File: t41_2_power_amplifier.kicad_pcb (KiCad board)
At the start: 2 copper layers, 69.5 x 93 mm, 52 parts, among them J1 5-1814832-1, J2 5-1814832-1, J3 B2B-XH-A_LF__SN_, J5 Screw_Terminal_01x02, Q1 Q_NMOS_GSD, Q3 Q_NMOS_GSD, T1 Transformer_1P_SS, T2 Transformer_1P_1S, T3 Transformer_1P_1S, U1 MCP1802x-xx02xOT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

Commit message: Version 1.7, release version to fab.
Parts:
- removed U1: MCP1802x-xx02xOT, Package_TO_SOT_SMD:SOT-23-5
- added R10: 2.2k, Resistor_SMD:R_1206_3216Metric, F.Cu at (143.9, 108.5)
- added U3: MCP1804x-A002xOT, Package_TO_SOT_SMD:SOT-23-5, F.Cu at (133.6, 113.6)
- C11: value 0.1uF -> 0.01uF
- C14: value 1uF -> 0.1uF
- moved C13 1.12 mm to (171.9, 116.3)
- moved C2 1.10 mm to (171.9, 113.2)
- moved R9 0.99 mm to (143.9, 111.5)
- moved C9 0.14 mm to (174.2, 121.4)
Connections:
- R9 pad 1: GND -> Net-(R10-Pad2)
- U2 pad 4: /TXRX -> GND
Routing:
- net Net-(R10-Pad2): track 0.00 -> 3.00 mm
- net /TXRX: track 22.8 -> 20.9 mm
- net Net-(U2-*OUT): track 19.8 -> 21.3 mm
- net Net-(U2-SET): track 5.57 -> 6.48 mm
- net GND: vias 122 -> 123
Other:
- board text added: "10 VOLTS"
- board text added: "V1.7"
- board text removed: "8 VOLTS"
- board text removed: "V1.6"

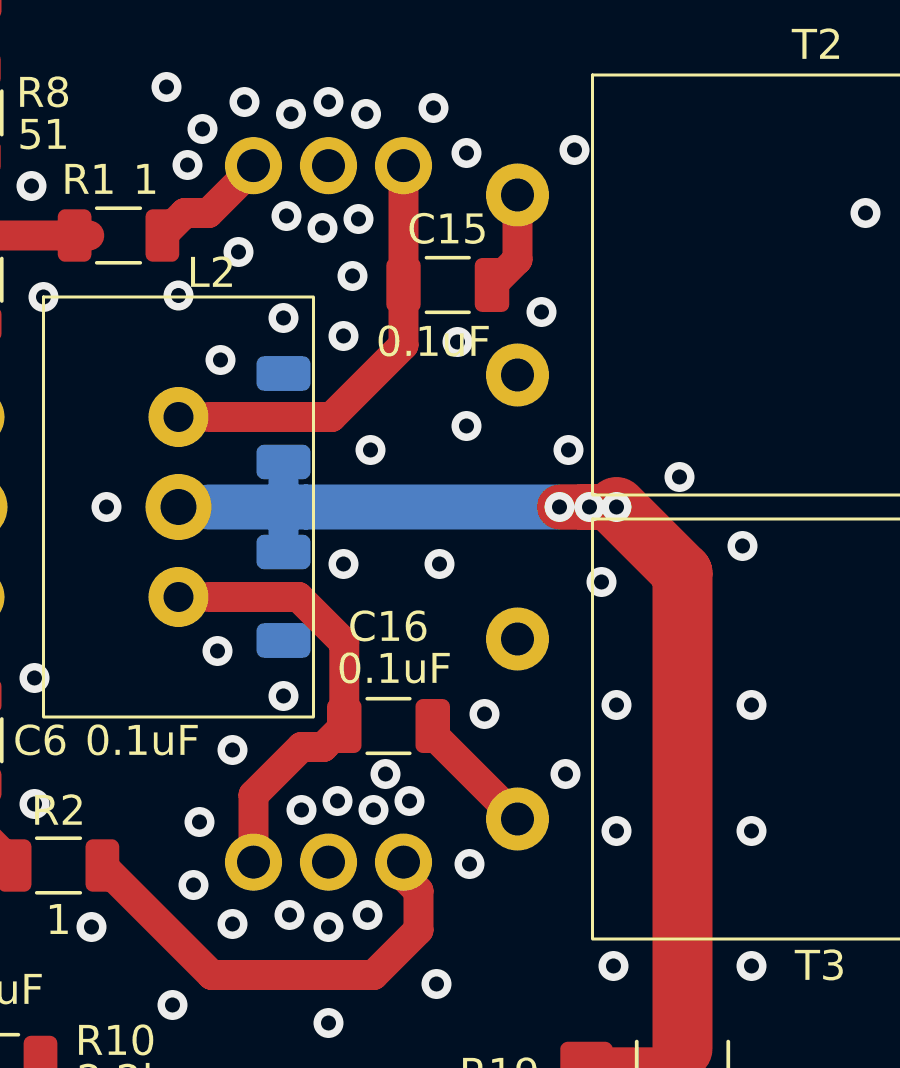
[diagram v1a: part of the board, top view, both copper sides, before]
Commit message: Added output tuning capacitor.
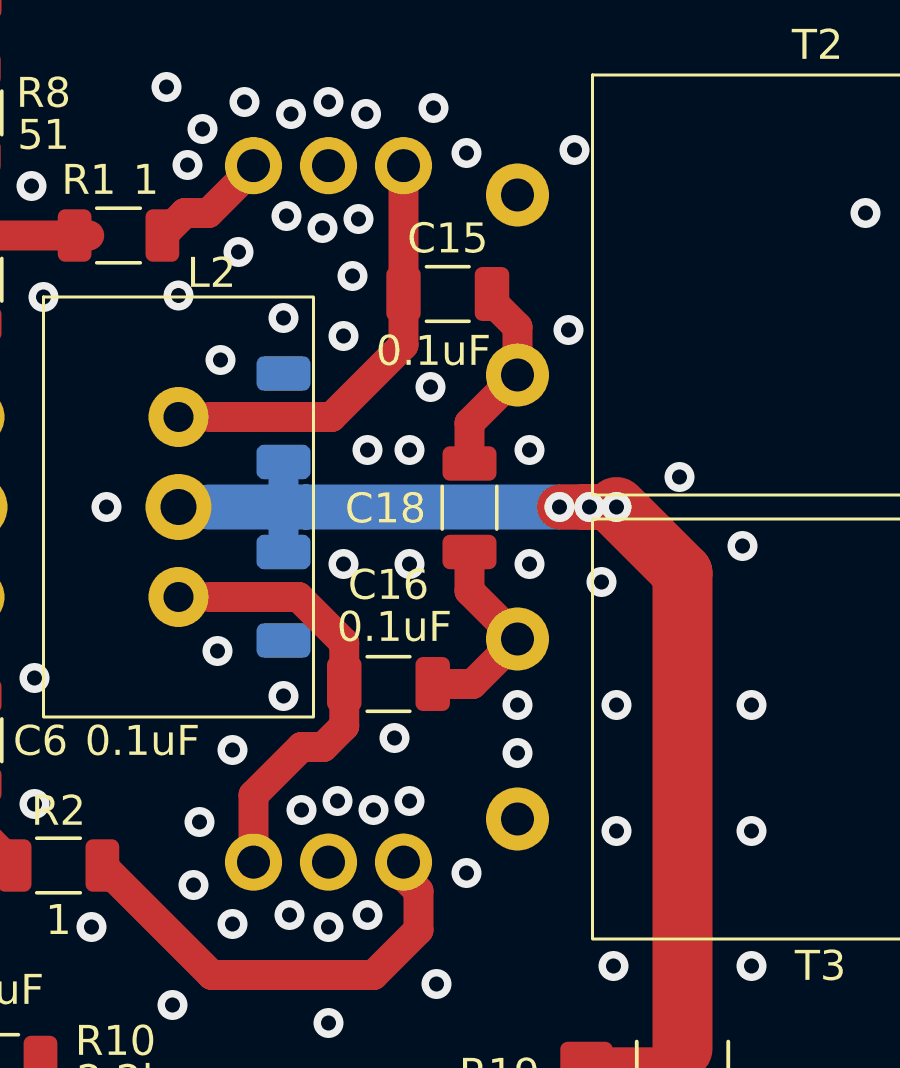
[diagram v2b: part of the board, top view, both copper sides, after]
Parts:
- added C18: 0.1uF, Capacitor_SMD:C_1206_3216Metric, F.Cu at (159.7, 90.0)
- moved C16 1.40 mm to (157.0, 95.9)
- moved C15 0.30 mm to (159.0, 82.9)
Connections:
- C15 pad 2: Net-(T2-AA) -> Net-(T2-AB)
- C16 pad 2: Net-(T3-AB) -> Net-(T3-AA)
- T2 pad 1: Net-(T2-AA) -> GND
- T2 pad 2: GND -> Net-(T2-AB)
- T3 pad 1: GND -> Net-(T3-AA)
- T3 pad 2: Net-(T3-AB) -> GND
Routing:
- net Net-(T3-AA): track 0.00 -> 7.01 mm
- net Net-(T2-AB): track 0.00 -> 6.66 mm
- net Net-(T3-AB): track 4.27 -> 0.00 mm
- net Net-(T2-AA): track 3.35 -> 0.00 mm
- net GND: vias 123 -> 124

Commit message: Initial commit to Github.
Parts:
- R10: value 2.2k -> 0
- U2: value MCP9509CT-E/OT -> MCP9509HT-E/OT
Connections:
- net /8V renamed /10V
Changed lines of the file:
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@@
 	(net 11 "/12V_FIL")
 	(net 12 "/TXRX")
-	(net 13 "/8V")
+	(net 13 "/10V")
 	(net 14 "Net-(T1-AA)")
 	(net 15 "Net-(D1-K)")
@@
 			(layers "*.Cu" "*.Mask")
 			(remove_unused_layers no)
-			(net 13 "/8V")
+			(net 13 "/10V")
 			(pinfunction "1")
 			(pintype "passive")
@@
 			(layers "F.Cu" "F.Mask" "F.Paste")
 			(roundrect_rratio 0.217391)
-			(net 13 "/8V")
+			(net 13 "/10V")
 			(pintype "passive")
 		)
@@
 			)
 		)
-		(property "Value" "MCP9509CT-E/OT"
+		(property "Value" "MCP9509HT-E/OT"
 			(at 0 0 90)
 			(unlocked yes)
@@
 			(layers "*.Cu" "*.Mask")
 			(remove_unused_layers no)
-			(net 13 "/8V")
+			(net 13 "/10V")
 			(pinfunction "1")
 			(pintype "passive")
@@
 			(layers "F.Cu" "F.Mask" "F.Paste")
 			(roundrect_rratio 0.25)
-			(net 13 "/8V")
+			(net 13 "/10V")
 			(pinfunction "VOUT")
 			(pintype "power_out")
@@
 			)
 		)
-		(property "Value" "2.2k"
+		(property "Value" "0"
 			(at 4.1525 0.61 0)
 			(layer "F.SilkS")
